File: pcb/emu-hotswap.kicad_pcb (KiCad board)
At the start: 2 copper layers, 157.8 x 118.3 mm, 77 parts, among them J1 TRRS, SW1 SW_Push, SW10 SW_Push, SW11 SW_Push, SW12 SW_Push, SW13 SW_Push, SW14 SW_Push, SW15 SW_Push, SW16 SW_Push, SW17 SW_Push, SW18 SW_Push, SW19 SW_Push, SW2 SW_Push, SW20 SW_Push, SW21 SW_Push, SW22 SW_Push, SW23 SW_Push, SW24 SW_Push, SW25 SW_Push, SW26 SW_Push, SW27 SW_Push, SW28 SW_Push, SW29 SW_Push, SW3 SW_Push, SW30 SW_Push, SW31 SW_Push, SW32 SW_Push, SW4 SW_Push, SW5 SW_Push, SW6 SW_Push, SW7 SW_Push, SW8 SW_Push, SW9 SW_Push, U1 ProMicro

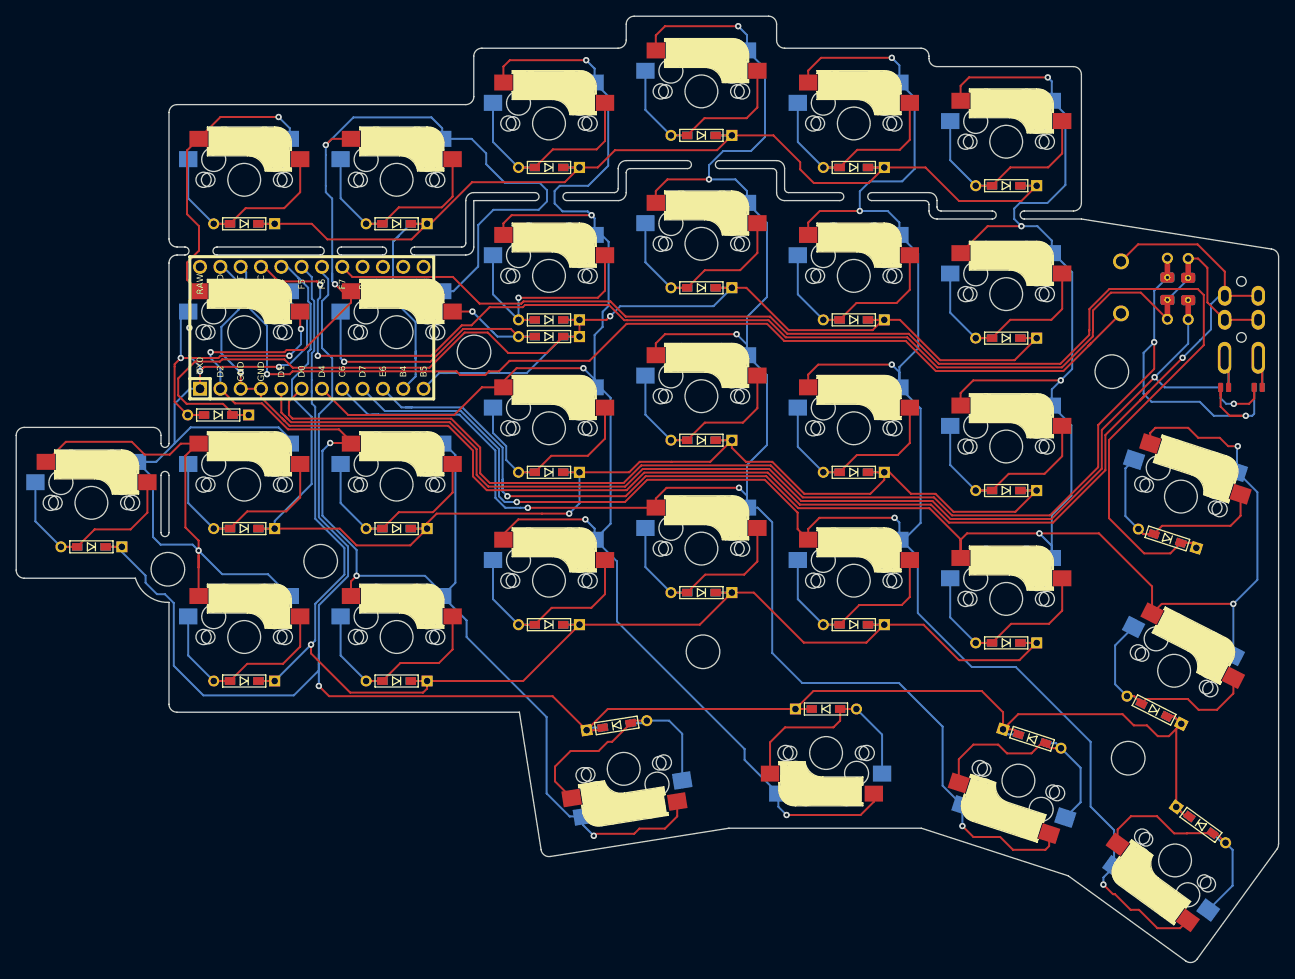
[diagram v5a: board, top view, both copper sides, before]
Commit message: Aligned everything to 0.05 grid.
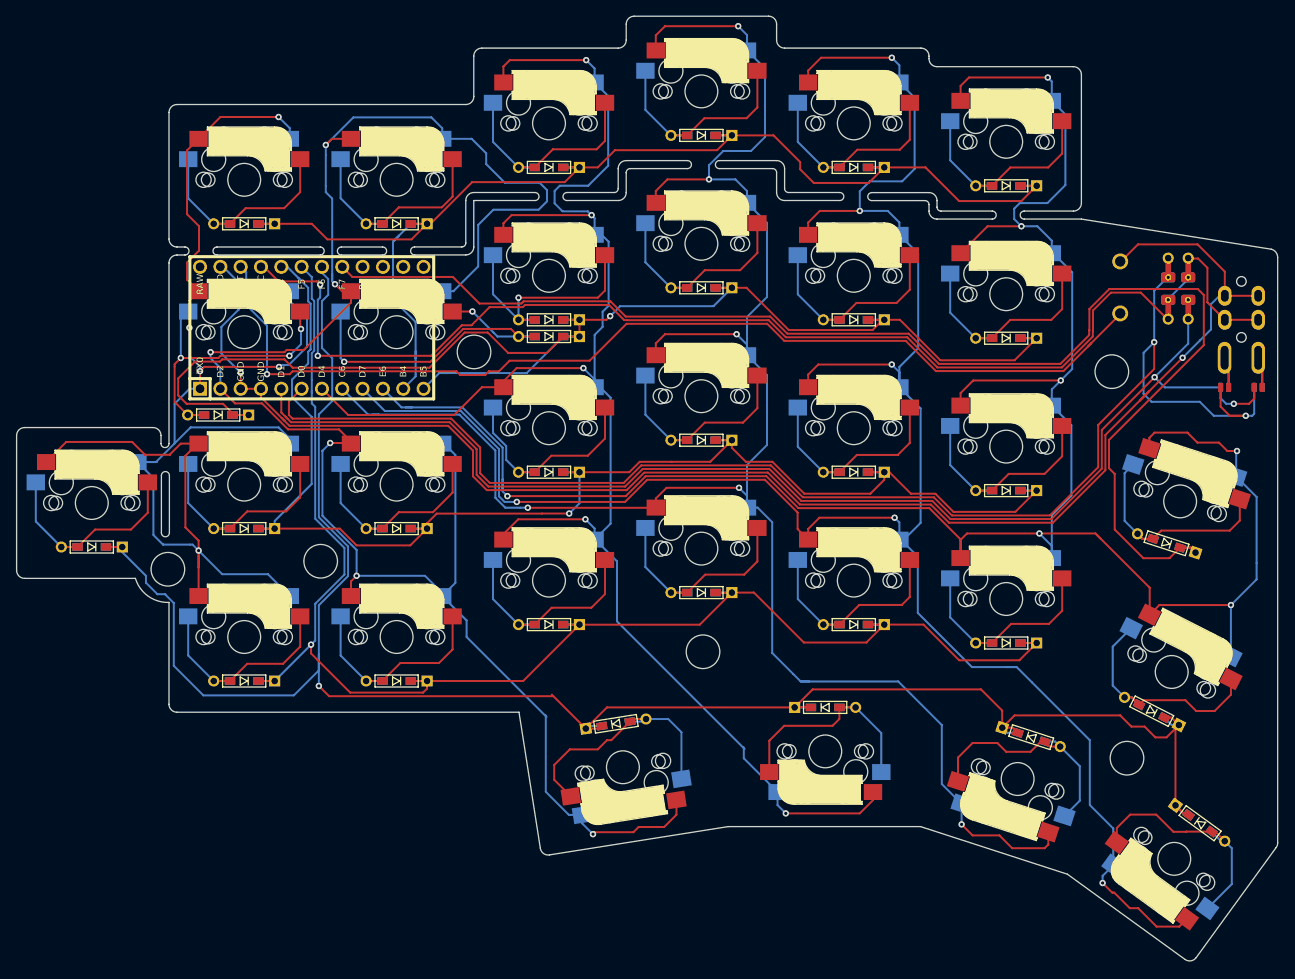
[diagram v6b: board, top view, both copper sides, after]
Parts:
- moved SW31 0.61 mm to (222.0, 91.2)
- moved D31 0.61 mm to (220.3, 96.4)
- moved D30 0.34 mm to (218.4, 117.4)
- moved SW30 0.34 mm to (220.9, 112.5)
- moved D25 0.22 mm to (224.5, 131.4)
- moved SW25 0.22 mm to (221.3, 135.9)
- moved D20 0.22 mm to (203.4, 120.7)
- moved D15 0.22 mm to (177.6, 117.0)
- moved SW10 0.22 mm to (152.3, 124.4)
- moved SW15 0.22 mm to (177.6, 122.5)
- moved SW20 0.22 mm to (201.7, 125.9)
- moved D10 0.22 mm to (151.5, 119.0)
- moved HM1 0.15 mm to (215.3, 123.3)
- moved R2 0.10 mm to (220.5, 64.6)
- moved SW32 0.10 mm to (214.5, 64.5)
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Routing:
- net /col4: track 271.3 -> 272.3 mm
- net /col3: track 248.4 -> 249.2 mm
- net /rowF: track 167.8 -> 168.4 mm
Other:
- board size 157.8 x 118.3 mm -> 157.6 x 118.1 mm
